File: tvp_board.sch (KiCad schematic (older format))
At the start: 87 parts, among them J1 VGA, J2 3XRCA_CONN, J3 SCART-F, J5 5VDC_IN, J6 SJ1-3533NG, J7 SJ1-3533NG, SW1 SPST, SW4 DPDT, U1 TVP7002PZP, U17 THS7353, U4 SN74LVC2G17, U5 AP7361C, U6 TLV70033, U7 NCP703SN19T1G, U9 TLV70019, Y1 ACHL-27MHZ-EK

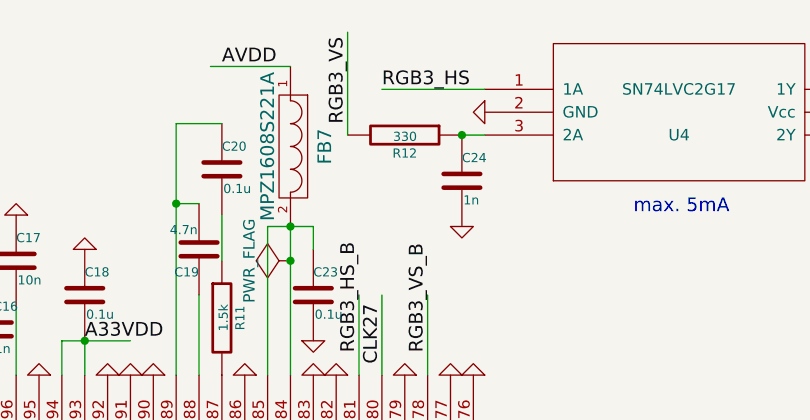
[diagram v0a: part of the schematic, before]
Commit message: Regenerate PCB files after recent small updates.
- update R12 value on schematic, netlist and layout.
- update ECS-3X9X footprint.
- add pdf of the schematic.
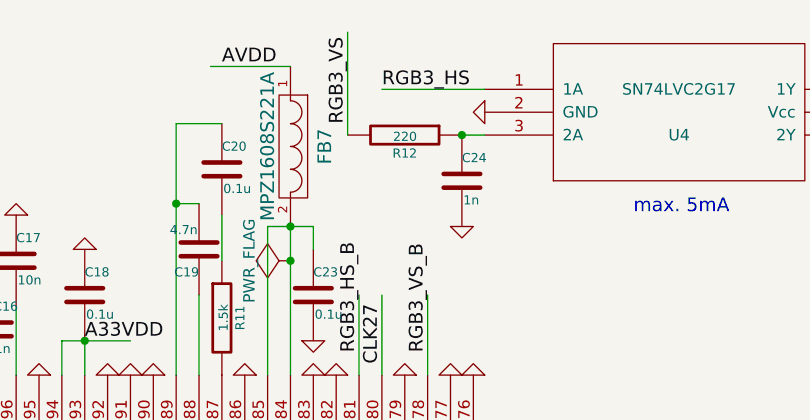
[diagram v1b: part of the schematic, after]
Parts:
- R12: value 330 -> 220
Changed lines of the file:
@@
 Sheet 3 4
 Title "Open Source Scan Converter"
-Date "2017-04-14"
+Date "2017-07-03"
 Rev "1.6"
 Comp ""
@@
 P 6700 1050
 F 0 "R12" V 6780 1050 40  0000 C CNN
-F 1 "330" V 6707 1051 40  0000 C CNN
+F 1 "220" V 6707 1051 40  0000 C CNN
 F 2 "custom_components:SM0603_Resistor_libcms" V 6630 1050 30  0001 C CNN
 F 3 "~" H 6700 1050 30  0000 C CNN

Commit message: - Update schematics and board to KiCAD 5.x
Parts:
- C1, C10, C100, C103, C104, C105, C106, C11, C12, C15, C2, C3, C33, C36, C4, C5, C6, C7, C76, C8, C9: symbol C -> ossc_board-rescue:C
- C107, C109, C13, C14, C16, C17, C18, C19, C20, C21, C22, C23, C24, C25, C26, C27, C28, C31, C32, C34, C35, C37, C38, C70, C71, C72, C93, C95: symbol C-RESCUE-ossc_board -> ossc_board-rescue:C-RESCUE-ossc_board
- D5: symbol ZENER -> ossc_board-rescue:ZENER
- F1: symbol F_Small -> ossc_board-rescue:F_Small
- FB5, FB6, FB7: symbol FILTER -> ossc_board-rescue:FILTER
- J1: symbol VGA -> ossc_board-rescue:VGA
- J2: symbol 3xRCA_CONN -> ossc_board-rescue:3xRCA_CONN
- J3: symbol SCART-F -> ossc_board-rescue:SCART-F
- J5: symbol BARREL_JACK -> ossc_board-rescue:BARREL_JACK
- J6, J7: symbol CONN_01X03 -> ossc_board-rescue:CONN_01X03
- R1, R10, R2, R3, R38, R4, R44, R5, R6, R7, R8, R9: symbol R -> ossc_board-rescue:R
- R11, R12, R13, R14, R15: symbol R-RESCUE-ossc_board -> ossc_board-rescue:R-RESCUE-ossc_board
- SW1: symbol SPST -> ossc_board-rescue:SPST
- SW4: symbol DPDT -> ossc_board-rescue:DPDT
- U1: symbol TVP7002 -> ossc_board-rescue:TVP7002
- U17: symbol THS7353 -> ossc_board-rescue:THS7353
- U4: symbol SN74LVC2G17 -> ossc_board-rescue:SN74LVC2G17
- U5: symbol SPX2920M3-3.3 -> ossc_board-rescue:SPX2920M3-3.3
- U6, U7, U9: symbol TLV71209DBV-RESCUE-ossc_board -> ossc_board-rescue:TLV71209DBV-RESCUE-ossc_board
- Y1: symbol ACHL-27MHZ-EK -> ossc_board-rescue:ACHL-27MHZ-EK

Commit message: update to Kicad 5.x symbols
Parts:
- C1, C10, C100, C103, C104, C105, C106, C11, C12, C15, C2, C3, C33, C36, C4, C5, C6, C7, C76, C8, C9: symbol ossc_board-rescue:C -> Device:C
- C107, C109, C13, C14, C16, C17, C18, C19, C20, C21, C22, C23, C24, C25, C26, C27, C28, C31, C32, C34, C35, C37, C38, C70, C71, C72, C93, C95: symbol ossc_board-rescue:C-RESCUE-ossc_board -> Device:C
- D5: symbol ossc_board-rescue:ZENER -> Device:D_Zener
- F1: symbol ossc_board-rescue:F_Small -> Device:Fuse_Small
- FB5, FB6, FB7: symbol ossc_board-rescue:FILTER -> Device:Ferrite_Bead
- J1: symbol ossc_board-rescue:VGA -> custom_components:VGA
- J2: symbol ossc_board-rescue:3xRCA_CONN -> custom_components:3xRCA_CONN
- J3: symbol ossc_board-rescue:SCART-F -> Connector:SCART-F
- J5: symbol ossc_board-rescue:BARREL_JACK -> Connector:Barrel_Jack_Switch
- J6, J7: symbol ossc_board-rescue:CONN_01X03 -> Connector_Generic:Conn_01x03
- R1, R10, R2, R3, R38, R4, R44, R5, R6, R7, R8, R9: symbol ossc_board-rescue:R -> Device:R
- R11, R12, R13, R14, R15: symbol ossc_board-rescue:R-RESCUE-ossc_board -> Device:R
- SW1: symbol ossc_board-rescue:SPST -> Switch:SW_SPST
- SW4: symbol ossc_board-rescue:DPDT -> custom_components:DPDT
- U1: symbol ossc_board-rescue:TVP7002 -> custom_components:TVP7002
- U17: symbol ossc_board-rescue:THS7353 -> custom_components:THS7353
- U4: symbol ossc_board-rescue:SN74LVC2G17 -> custom_components:SN74LVC2G17
- U5: symbol ossc_board-rescue:SPX2920M3-3.3 -> Regulator_Linear:AP7361C-33E
- U6: symbol ossc_board-rescue:TLV71209DBV-RESCUE-ossc_board -> Regulator_Linear:TLV70033_SOT23-5
- U7: symbol ossc_board-rescue:TLV71209DBV-RESCUE-ossc_board -> Regulator_Linear:NCP718xSN180
- U9: symbol ossc_board-rescue:TLV71209DBV-RESCUE-ossc_board -> Regulator_Linear:TLV70019_SOT23-5
- Y1: symbol ossc_board-rescue:ACHL-27MHZ-EK -> custom_components:ACHL-27MHZ-EK
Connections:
- wire segments 237 -> 294
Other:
- moved on the sheet: C107, C14, C18, C20, C21, C22, C23, C24, C25, C26, C27, C28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

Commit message: update to pcb v1.7
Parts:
- removed D5: SD05-7, custom_components:SOD-323_Handsoldering, symbol Device:D_Zener
- added C117, C122: 10u, custom_components:SM0603_Capa_libcms, symbol Device:C_Small
- added D10, D8, D9: PESD5V0U4BW, Package_TO_SOT_SMD:SOT-665, symbol custom_components:PESD5V0U4BW
- added D11, D12, D5: PESD12VL2BT, Package_TO_SOT_SMD:SOT-23_Handsoldering, symbol custom_components:PESD12VL2BT
- added D13: PESD5V0V4UW, Package_TO_SOT_SMD:SOT-665, symbol custom_components:PESD5V0V4UW
- added D14: BZX84C5V1/SOT, Package_TO_SOT_SMD:SOT-23_Handsoldering, symbol Device:D_Schottky
- added L1: 2.2u, custom_components:CDRH2D14, symbol Device:L_Small
- added Q3, Q5: AOSS21115C, Package_TO_SOT_SMD:SOT-23_Handsoldering, symbol Device:Q_PMOS_GSD
- added Q4: DSS20200L, Package_TO_SOT_SMD:SOT-23_Handsoldering, symbol Device:Q_PNP_BEC
- added R53, R54: 27k, custom_components:SM0603_Resistor_libcms, symbol Device:R_Small
- added R55: 330, custom_components:SM0805_libcms, symbol Device:R_Small
- added R56, R58: 6.8k, custom_components:SM0603_Resistor_libcms, symbol Device:R_Small
- added R57: 100k, custom_components:SM0603_Resistor_libcms, symbol Device:R_Small
- added U18: LM3671MF-2.5/NOPB, custom_components:SOT-23-5_Handsoldering, symbol Regulator_Switching:LM3670MF
- F1: value F0603E1R50FSTR -> F0603E1R25FSTR
- SW4: value DPDT -> GW22RCV; footprint custom_components:MS22 -> custom_components:GW22RxV
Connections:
- net labels added: DVDD2V5
- wire segments 294 -> 349
- no-connect marks 22 -> 26
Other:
- note added: "<= 368mA (max. 600mA)"
- note added: "<=111mA (max. 200mA)"
- note added: "<=279mA (max. 300mA)"
- note added: "<=589mA (max. 1000mA)"
- note added: "<=89mA (max. 200mA)"
- note added: "Total from 5V rail:\n589mA+111mA+\n((2.5V/5V)*368mA)/0.9\n<=904mA"
- note added: "overvoltage protection, Vth = 5.5V"
- note added: "reverse current\nprotection"
- note removed: "max. 1000mA"
- note removed: "max. 200mA"
- note removed: "max. 300mA"
- note removed: "max. 957mA+111mA\n=1068mA drawn"
- moved on the sheet: C107, C109, C12, C21, C22, C24, C25, C3, C31, C32, C33, C35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

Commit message: fix D14 footprint and add RoHS & WEEE logos
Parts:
- D14: footprint Package_TO_SOT_SMD:SOT-23_Handsoldering -> Diode_SMD:D_SOT-23_ANK
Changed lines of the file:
@@
 F 0 "D14" V 6604 6880 50  0000 L CNN
 F 1 "BZX84C5V1/SOT" V 6695 6880 50  0000 L CNN
-F 2 "Package_TO_SOT_SMD:SOT-23_Handsoldering" H 6650 6800 50  0001 C CNN
+F 2 "Diode_SMD:D_SOT-23_ANK" H 6650 6800 50  0001 C CNN
 F 3 "~" H 6650 6800 50  0001 C CNN
 	1    6650 6800
